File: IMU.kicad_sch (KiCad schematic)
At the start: 6 parts, among them U2 BNO055

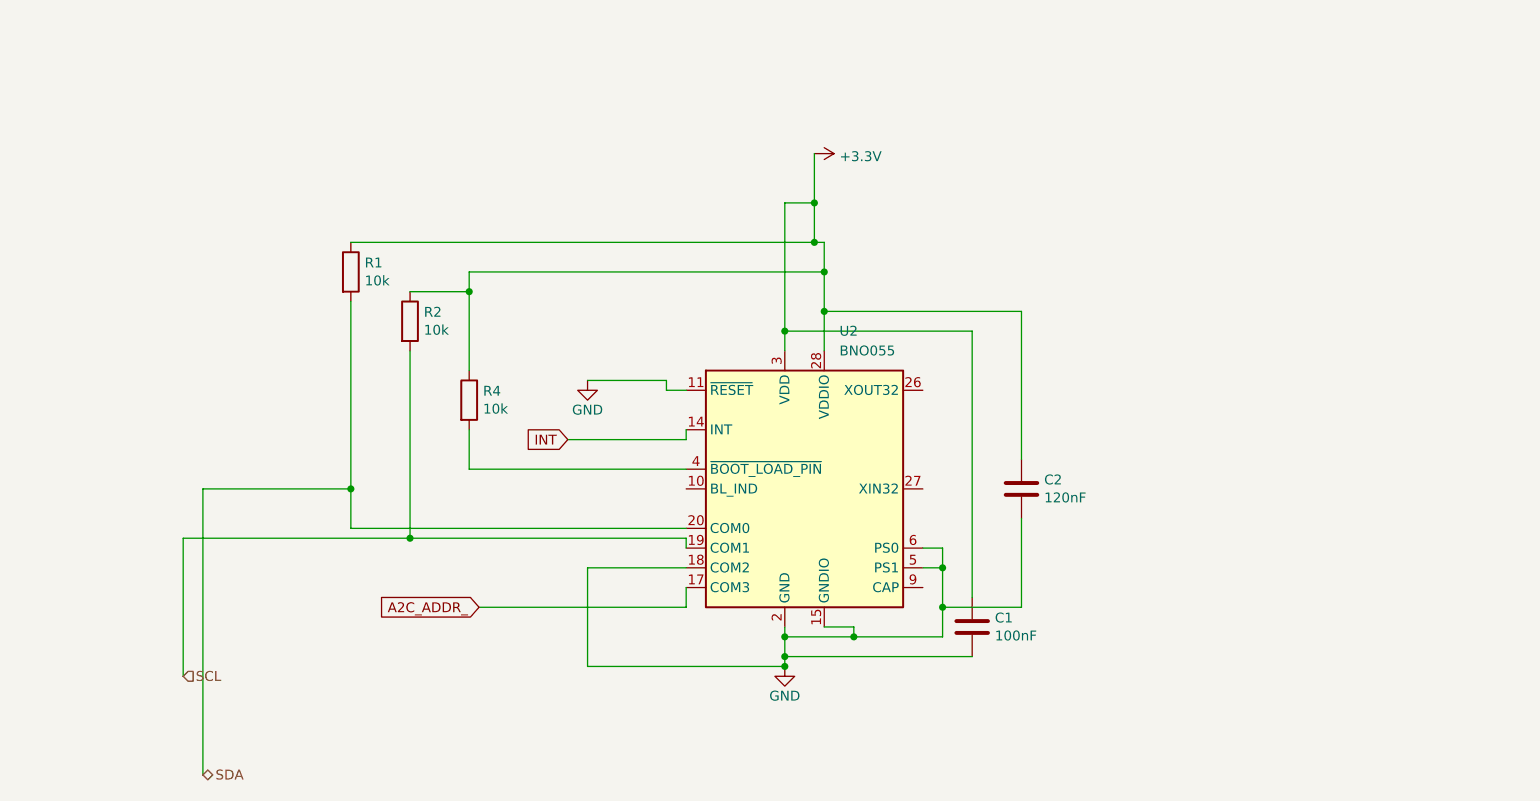
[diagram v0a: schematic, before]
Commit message: Magnetometer fixes\n\nCloses #2
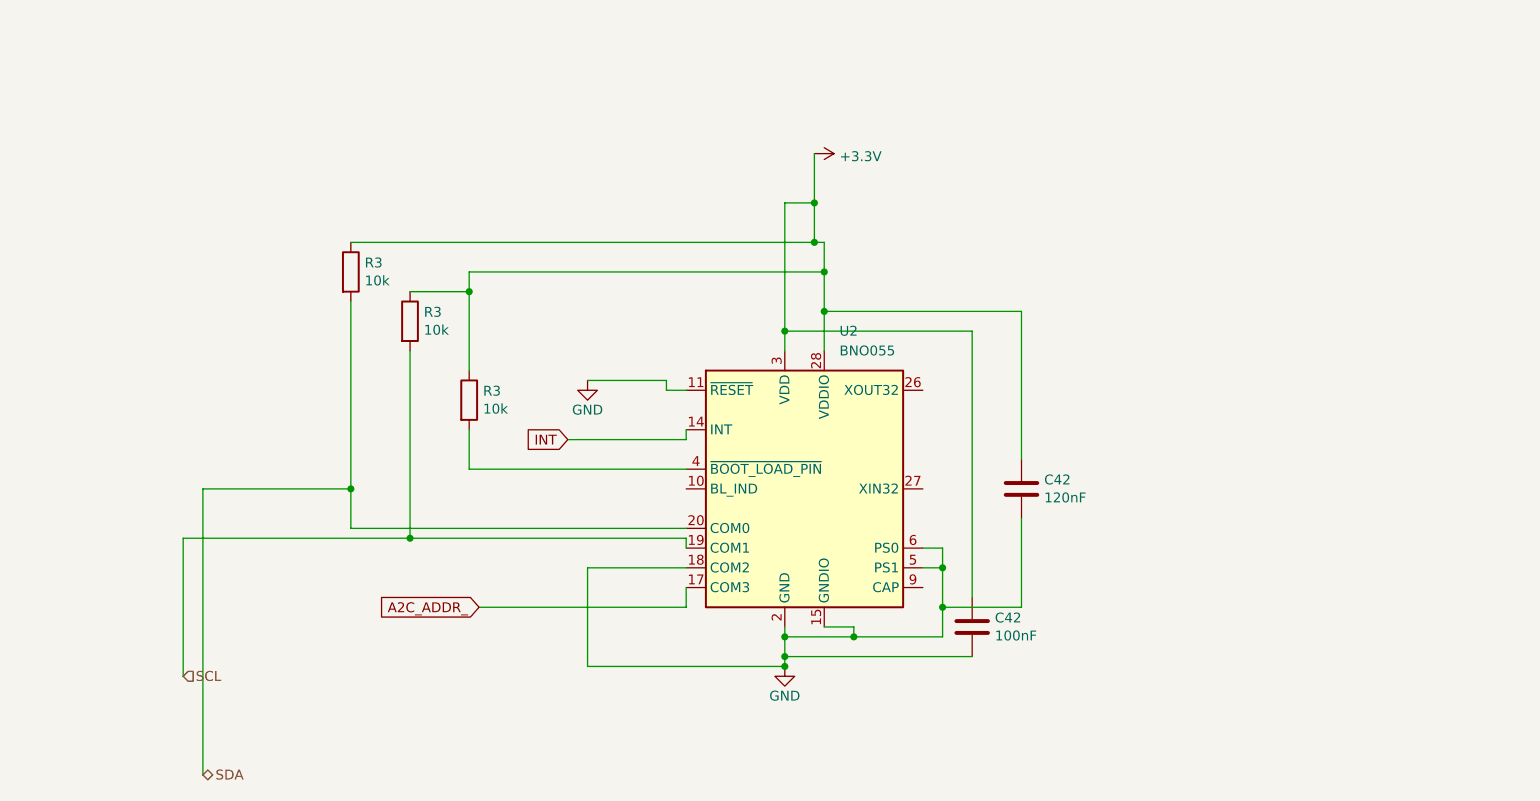
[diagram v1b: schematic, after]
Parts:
- renumbered C1 to C42, C2 to C42, R1 to R3, R4 to R3, R2 to R3
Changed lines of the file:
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@@
   (symbol (lib_id "Device:R") (at 95.25 58.42 0) (unit 1)
     (in_bom yes) (on_board yes) (dnp no)
-    (property "Reference" "R1" (at 97.028 57.2516 0)
+    (property "Reference" "R3" (at 97.028 57.2516 0)
       (effects (font (size 1.27 1.27)) (justify left))
     )
@@
   (symbol (lib_id "Device:C") (at 175.26 104.14 0) (unit 1)
     (in_bom yes) (on_board yes) (dnp no)
-    (property "Reference" "C1" (at 178.181 102.9716 0)
+    (property "Reference" "C42" (at 178.181 102.9716 0)
       (effects (font (size 1.27 1.27)) (justify left))
     )
@@
   (symbol (lib_id "power:GND") (at 125.73 72.39 0) (unit 1)
     (in_bom yes) (on_board yes) (dnp no)
-    (property "Reference" "#PWR01" (at 125.73 78.74 0)
+    (property "Reference" "#PWR033" (at 125.73 78.74 0)
       (effects (font (size 1.27 1.27)) hide)
     )
@@
   (symbol (lib_id "power:GND") (at 151.13 109.22 0) (unit 1)
     (in_bom yes) (on_board yes) (dnp no)
-    (property "Reference" "#PWR02" (at 151.13 115.57 0)
+    (property "Reference" "#PWR033" (at 151.13 115.57 0)
       (effects (font (size 1.27 1.27)) hide)
     )
@@
   (symbol (lib_id "Device:R") (at 110.49 74.93 0) (unit 1)
     (in_bom yes) (on_board yes) (dnp no)
-    (property "Reference" "R4" (at 112.268 73.7616 0)
+    (property "Reference" "R3" (at 112.268 73.7616 0)
       (effects (font (size 1.27 1.27)) (justify left))
     )
@@
   (symbol (lib_id "Device:R") (at 102.87 64.77 0) (unit 1)
     (in_bom yes) (on_board yes) (dnp no)
-    (property "Reference" "R2" (at 104.648 63.6016 0)
+    (property "Reference" "R3" (at 104.648 63.6016 0)
       (effects (font (size 1.27 1.27)) (justify left))
     )
@@
   (symbol (lib_id "Device:C") (at 181.61 86.36 0) (unit 1)
     (in_bom yes) (on_board yes) (dnp no)
-    (property "Reference" "C2" (at 184.531 85.1916 0)
-      (effects (font (size 1.27 1.27)) (justify left))
-    )
+    (property "Reference" "C42" (at 184.531 85.1916 0)
+      (effects (font (size 1.27 1.27)) (justify left))
+    )

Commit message: IMU schematic fixes
Closes #3
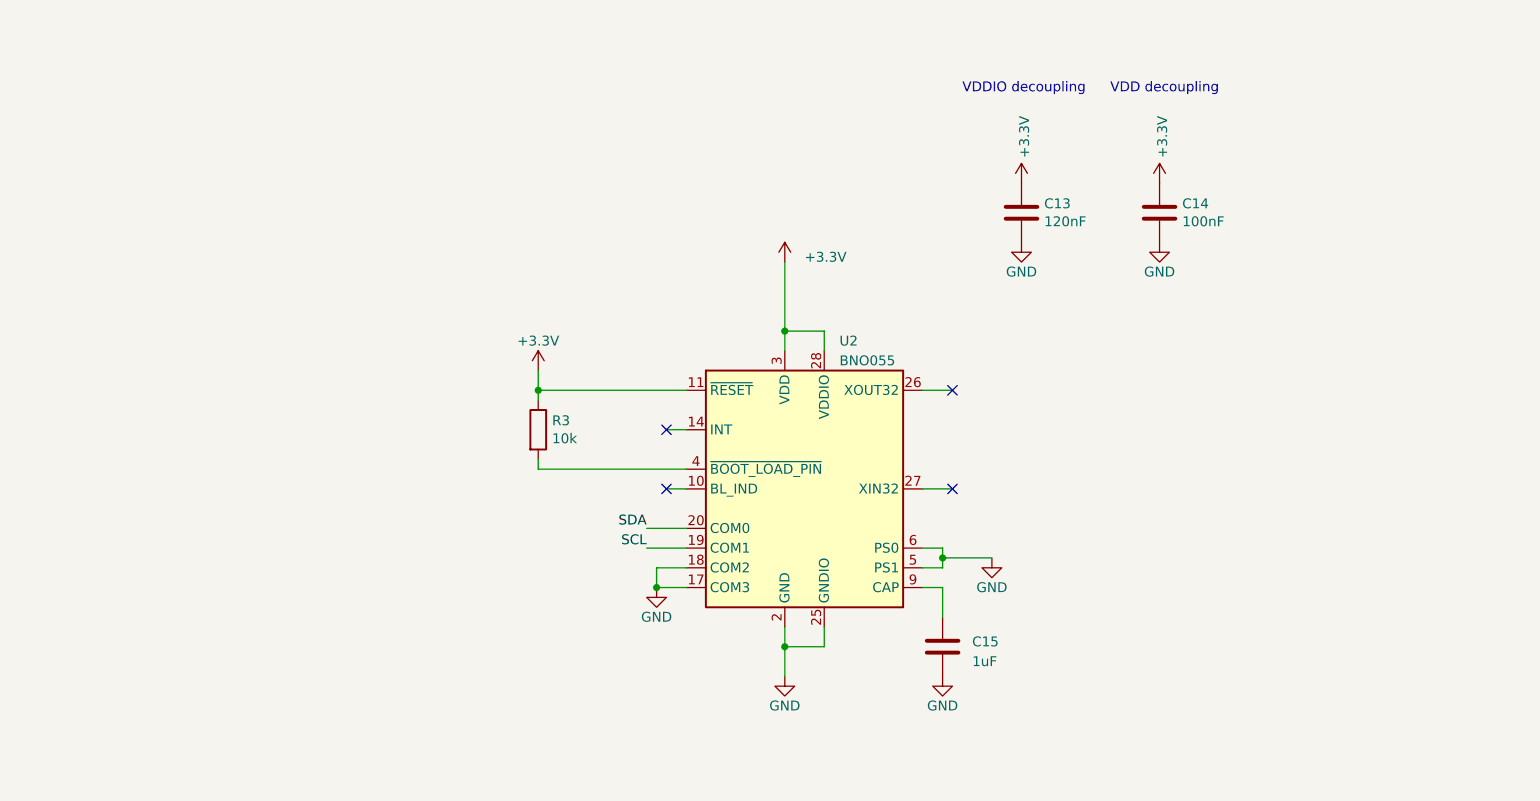
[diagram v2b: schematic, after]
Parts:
- removed C42: 100nF, Capacitor_SMD:C_0603_1608Metric, symbol Device:C
- removed C42: 120nF, Capacitor_SMD:C_0603_1608Metric, symbol Device:C
- removed R3 (x2): 10k, Resistor_SMD:R_0603_1608Metric_Pad1.05x0.95mm_HandSolder, symbol Device:R
- added C13: 120nF, Capacitor_SMD:C_0603_1608Metric, symbol Device:C
- added C14: 100nF, Capacitor_SMD:C_0603_1608Metric, symbol Device:C
- added C15: 1uF, symbol Device:C
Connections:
- net A2C_ADDR_ is gone; now on net GND: U2.17 (COM3)
- net +3V3: now also U2.11 (~{RESET}), C13.1, C14.1
- net GND: now also C13.2, C14.2, C15.2; no longer U2.11 (~{RESET})
- net at U2.9 (CAP): now also C15.1
- net INT: no longer names the net of U2.14 (INT)
- no-connect marks 0 -> 4
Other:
- note added: "VDD decoupling"
- note added: "VDDIO decoupling"
- moved on the sheet: R3

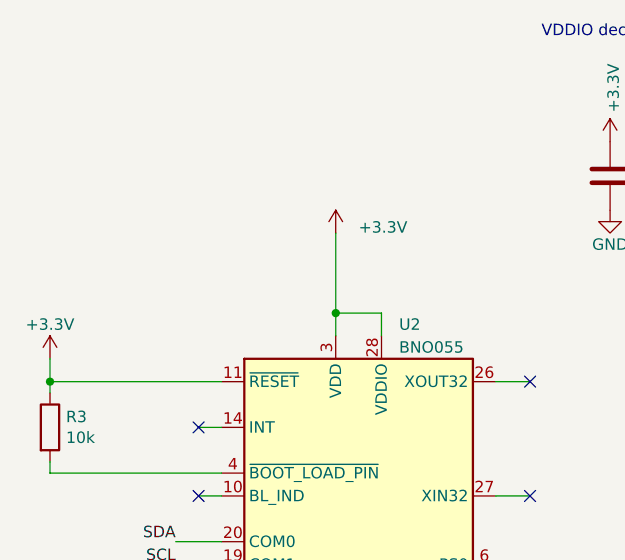
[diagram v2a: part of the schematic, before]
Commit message: Clean-up schematic
Closes #4
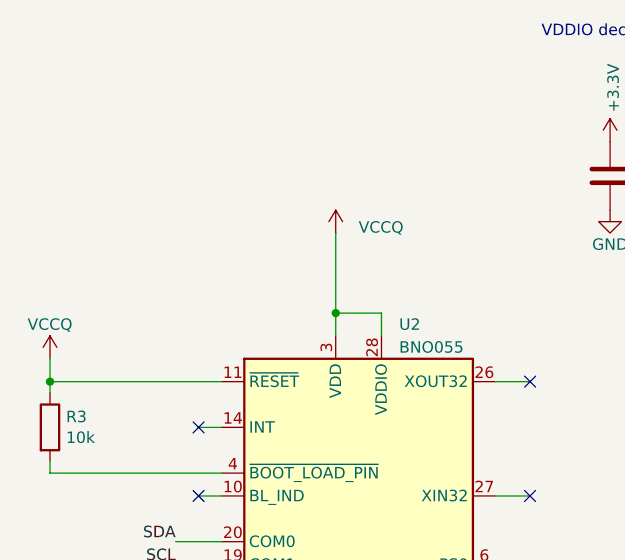
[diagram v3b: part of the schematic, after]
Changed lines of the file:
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@@
       (effects (font (size 1.27 1.27)) hide)
     )
-    (property "Value" "+3.3V" (at 119.38 67.31 0)
+    (property "Value" "VCCQ" (at 119.38 67.31 0)
       (effects (font (size 1.27 1.27)))
     )
@@
       (effects (font (size 1.27 1.27)) hide)
     )
-    (property "Value" "+3.3V" (at 153.67 56.515 0)
-      (effects (font (size 1.27 1.27)) (justify left))
-    )
+    (property "Value" "VCCQ" (at 153.67 56.515 0)
+      (effects (font (size 1.27 1.27)) (justify left))
+    )

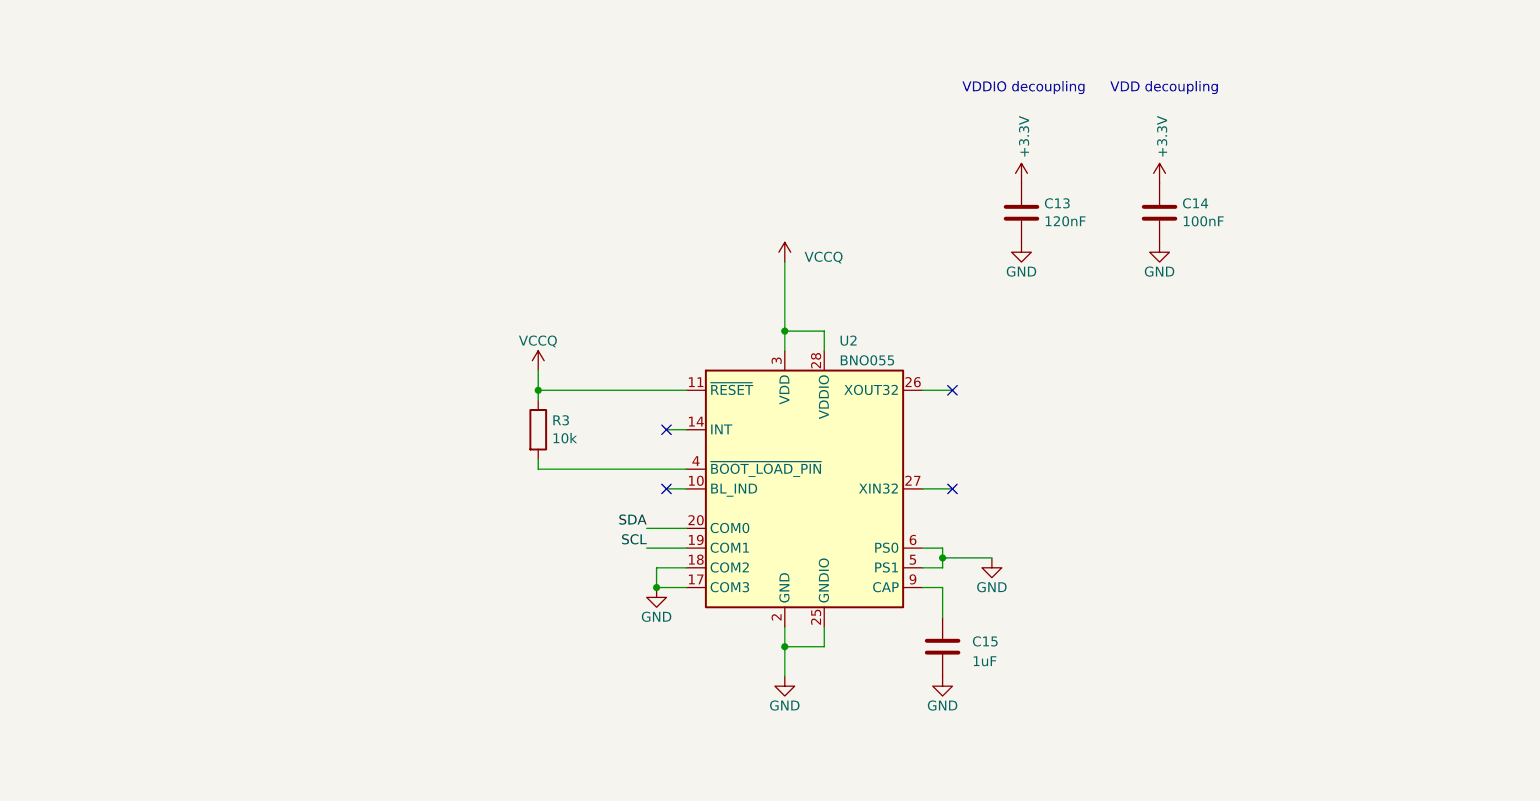
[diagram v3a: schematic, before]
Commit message: Add I2C multiplexer
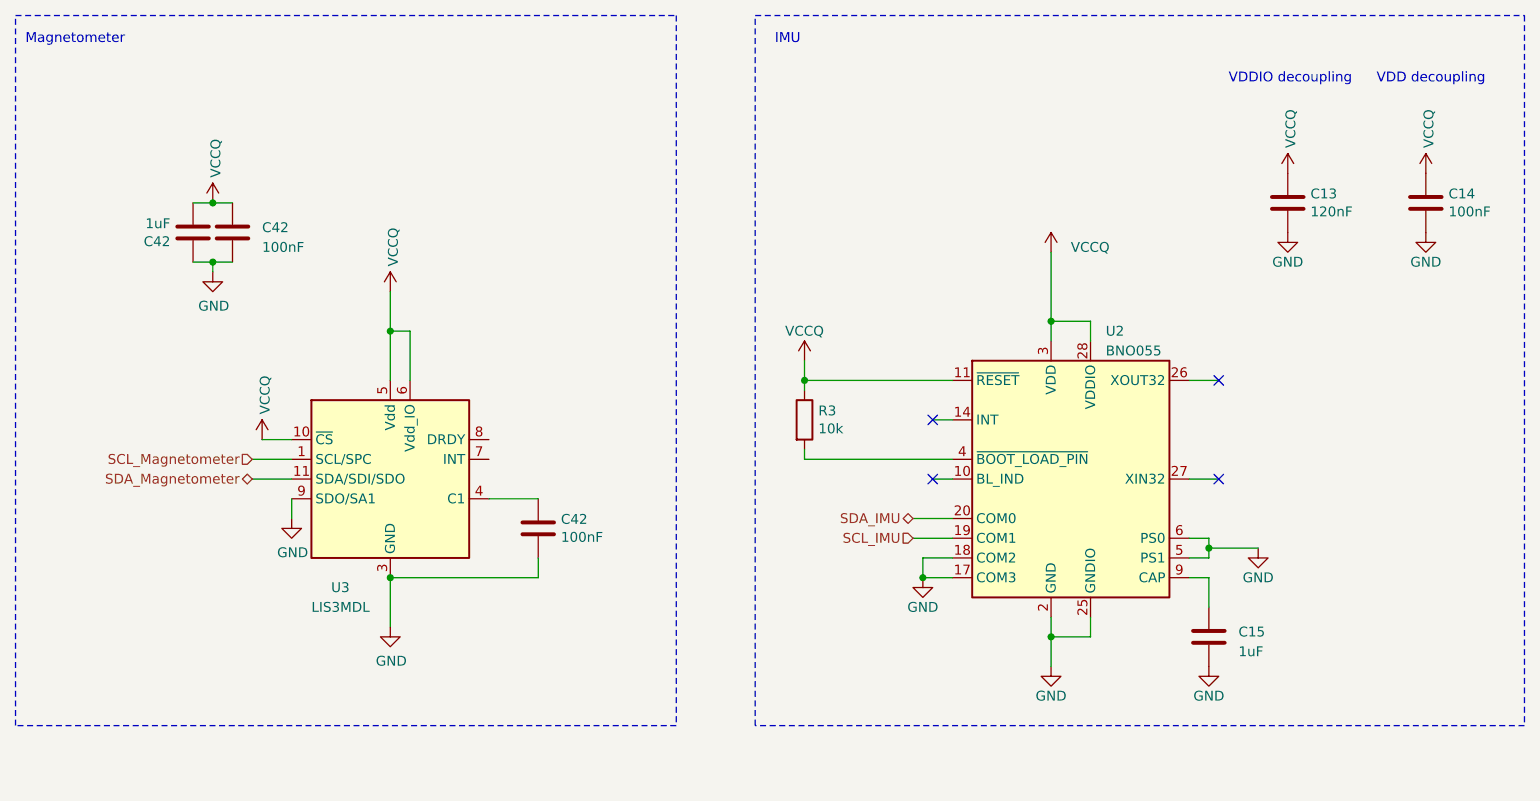
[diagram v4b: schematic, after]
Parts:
- added C42 (x2): 100nF, Capacitor_SMD:C_0603_1608Metric, symbol Device:C
- added C42: 1uF, Capacitor_SMD:C_0603_1608Metric, symbol Device:C
- added U3: LIS3MDL, Package_LGA:LGA-12_2x2mm_P0.5mm, symbol Sensor_Magnetic:LIS3MDL
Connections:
- net +3V3: now also C42.2, C42.2, U3.10 (~{CS}), U3.5 (Vdd), U3.6 (Vdd_IO)
- net GND: now also C42.1, C42.1, C42.2, U3.12 (GND), U3.2 (GND), U3.3 (GND), U3.9 (SDO/SA1)
- net SCL renamed SCL_IMU
- net SDA renamed SDA_IMU
- new net: C42.1, U3.4 (C1)
- new net SCL_Magnetometer: U3.1 (SCL/SPC)
- new net SDA_Magnetometer: U3.11 (SDA/SDI/SDO)
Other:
- note added: "IMU"
- note added: "Magnetometer"
- moved on the sheet: C13, C14, C15, R3, U2
